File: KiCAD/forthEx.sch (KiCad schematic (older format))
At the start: 33 parts, among them CON1 BARREL_JACK 2,1mm, J1 RCA_JACK, J2 RCA_JACK, J3 PS/2, P1 ICSP, SW1 Power, SW2 reset, U1 LD33V, U2 PIC24FJ64GA002, U3 25LC512, X1 8Mhz

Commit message: first commit
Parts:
- added C12: 100nF, ~, symbol C
- added C7: 10nF, ~, symbol C
- added C8: 22nF, ~, symbol C
- added J3: USB-A_F, symbol USB-A_F
- added R12: 10k, ~, symbol R
- added R7: 4k7, ~, symbol R
- added U4: 23LC1024, symbol 23LC512
- C3, C4: value 22pF -> 18pF
- R9: renamed from R7; value 10K -> 4k7
- U1: value LD33V -> LD1117v33
- U3: value 25LC512 -> 25LC1024
- renumbered C8 to C10, C9 to C11, C7 to C9, J3 to J4, R9 to R10, R10 to R11, R11 to R13, R5 to R2, R2 to R3, R8 to R4, R3 to R5, R4 to R6, R6 to R8
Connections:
- net labels added: ~SS1, ~SS2
- net labels removed: ~SS
- wire segments 104 -> 126
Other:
- note added: "connecteur clavier\n"
- note added: "option 1"
- note added: "option 2"
- moved on the sheet: J1, J4, U3

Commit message: travail sur tvout.s
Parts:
- added D1: 1N6263, symbol DIODESCH
- renumbered D1 to D2, R8 to R10, R7 to R6, R9 to R7, R10 to R8, R6 to R9
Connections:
- wire segments 126 -> 127
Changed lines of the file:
@@
 $EndComp
 $Comp
-L R R9
+L R R7
 U 1 1 55772335
 P 5250 5000
-F 0 "R9" V 5330 5000 40  0000 C CNN
+F 0 "R7" V 5330 5000 40  0000 C CNN
 F 1 "4k7" V 5257 5001 40  0000 C CNN
 F 2 "~" V 5180 5000 30  0000 C CNN
@@
 $EndComp
 $Comp
-L R R6
+L R R9
 U 1 1 557C98D1
 P 7100 2800
-F 0 "R6" V 7180 2800 40  0000 C CNN
+F 0 "R9" V 7180 2800 40  0000 C CNN
 F 1 "10K" V 7107 2801 40  0000 C CNN
 F 2 "~" V 7030 2800 30  0000 C CNN
@@
 $EndComp
 $Comp
-L R R8
+L R R10
 U 1 1 557C98D7
 P 7300 2800
-F 0 "R8" V 7380 2800 40  0000 C CNN
+F 0 "R10" V 7380 2800 40  0000 C CNN
 F 1 "10K" V 7307 2801 40  0000 C CNN
 F 2 "~" V 7230 2800 30  0000 C CNN
@@
 $EndComp
 $Comp
-L LED D1
+L LED D2
 U 1 1 557C9D7F
 P 2800 3200
-F 0 "D1" H 2800 3300 50  0000 C CNN
+F 0 "D2" H 2800 3300 50  0000 C CNN
 F 1 "LED" H 2800 3100 50  0000 C CNN
 F 2 "~" H 2800 3200 60  0000 C CNN
@@
 $EndComp
 $Comp
-L R R10
+L R R8
 U 1 1 557F975C
 P 6000 5250
-F 0 "R10" V 6080 5250 40  0000 C CNN
+F 0 "R8" V 6080 5250 40  0000 C CNN
 F 1 "1K" V 6007 5251 40  0000 C CNN
 F 2 "~" V 5930 5250 30  0000 C CNN
@@
 Text GLabel 4500 3600 0    39   Input ~ 0
 Vidout
-Text GLabel 3000 5900 0    39   Input ~ 0
+Text GLabel 2450 5900 0    39   Input ~ 0
 Vidout
 $Comp
@@
 $EndComp
 $Comp
-L R R7
+L R R6
 U 1 1 5601461A
 P 4750 4550
-F 0 "R7" V 4830 4550 40  0000 C CNN
+F 0 "R6" V 4830 4550 40  0000 C CNN
 F 1 "4k7" V 4757 4551 40  0000 C CNN
 F 2 "~" V 4680 4550 30  0000 C CNN
@@
 	4500 3600 4900 3600
 Wire Wire Line
-	3000 5900 3150 5900
+	2950 5900 3150 5900
 Wire Wire Line
 	6400 3000 6250 3000
@@
 	7300 2350 7300 2550
 Connection ~ 7100 2350
+$Comp
+L DIODESCH D1
+U 1 1 56081043
+P 2750 5900
+F 0 "D1" H 2750 6000 50  0000 C CNN
+F 1 "1N6263" H 2750 5800 50  0000 C CNN
+F 2 "" H 2750 5900 60  0000 C CNN
+F 3 "" H 2750 5900 60  0000 C CNN
+	1    2750 5900
+	1    0    0    -1
+$EndComp
+Wire Wire Line
+	2450 5900 2550 5900
 $EndSCHEMATC

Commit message: travail sur keyboard.s
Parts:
- J4: value PS/2 -> miniDIN-6
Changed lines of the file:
@@
 LIBS:valves
 LIBS:forthEx-cache
-EELAYER 25 0
+EELAYER 27 0
 EELAYER END
 $Descr A4 11693 8268
@@
 Sheet 1 1
 Title ""
-Date "12 sep 2015"
+Date "2 oct 2015"
 Rev ""
 Comp ""
@@
 P 8750 2000
 F 0 "J4" H 8750 1650 60  0000 C CNN
-F 1 "PS/2" H 8750 2450 60  0000 C CNN
+F 1 "miniDIN-6" H 8750 2450 60  0000 C CNN
 F 2 "~" H 8750 2000 60  0000 C CNN
 F 3 "~" H 8750 2000 60  0000 C CNN

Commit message: schematic
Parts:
- removed U2: PIC24FJ64GA002, symbol PIC24FJ64GA002
- added U?: PIC24FJ64GA002, symbol PIC24FJ64GA002
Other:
- moved on the sheet: C10, U1
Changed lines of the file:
@@
 LIBS:valves
 LIBS:forthEx-cache
-EELAYER 27 0
+EELAYER 25 0
 EELAYER END
 $Descr A4 11693 8268
@@
 $EndDescr
 $Comp
-L PIC24FJ64GA002 U2
-U 1 1 5577231C
-P 5600 3750
-F 0 "U2" H 5600 3000 60  0000 C CNN
-F 1 "PIC24FJ64GA002" H 5600 4650 60  0000 C CNN
-F 2 "" H 5600 3750 60  0000 C CNN
-F 3 "" H 5600 3750 60  0000 C CNN
-	1    5600 3750
-	1    0    0    -1
-$EndComp
-$Comp
 L R R7
 U 1 1 55772335
@@
 L C C9
 U 1 1 55772ECC
-P 6750 2650
-F 0 "C9" H 6750 2750 40  0000 L CNN
-F 1 "100nF" H 6756 2565 40  0000 L CNN
-F 2 "~" H 6788 2500 30  0000 C CNN
-F 3 "~" H 6750 2650 60  0000 C CNN
-	1    6750 2650
+P 6900 2650
+F 0 "C9" H 6900 2750 40  0000 L CNN
+F 1 "100nF" H 6906 2565 40  0000 L CNN
+F 2 "~" H 6938 2500 30  0000 C CNN
+F 3 "~" H 6900 2650 60  0000 C CNN
+	1    6900 2650
 	0    -1   -1   0
 $EndComp
@@
 L GND #PWR18
 U 1 1 55772ED2
-P 6950 2850
-F 0 "#PWR18" H 6950 2850 30  0001 C CNN
-F 1 "GND" H 6950 2780 30  0001 C CNN
-F 2 "" H 6950 2850 60  0000 C CNN
-F 3 "" H 6950 2850 60  0000 C CNN
-	1    6950 2850
+P 7100 2850
+F 0 "#PWR18" H 7100 2850 30  0001 C CNN
+F 1 "GND" H 7100 2780 30  0001 C CNN
+F 2 "" H 7100 2850 60  0000 C CNN
+F 3 "" H 7100 2850 60  0000 C CNN
+	1    7100 2850
 	1    0    0    -1
 $EndComp
@@
 L CAPAPOL C10
 U 1 1 55773066
-P 6850 3800
-F 0 "C10" H 6900 3900 40  0000 L CNN
-F 1 "47µF" H 6900 3700 40  0000 L CNN
-F 2 "~" H 6950 3650 30  0000 C CNN
-F 3 "~" H 6850 3800 300 0000 C CNN
-	1    6850 3800
+P 7000 3800
+F 0 "C10" H 7050 3900 40  0000 L CNN
+F 1 "47µF" H 7050 3700 40  0000 L CNN
+F 2 "~" H 7100 3650 30  0000 C CNN
+F 3 "~" H 7000 3800 300 0000 C CNN
+	1    7000 3800
 	0    -1   -1   0
 $EndComp
@@
 L GND #PWR19
 U 1 1 55773073
-P 7200 4150
-F 0 "#PWR19" H 7200 4150 30  0001 C CNN
-F 1 "GND" H 7200 4080 30  0001 C CNN
-F 2 "" H 7200 4150 60  0000 C CNN
-F 3 "" H 7200 4150 60  0000 C CNN
-	1    7200 4150
+P 7350 4150
+F 0 "#PWR19" H 7350 4150 30  0001 C CNN
+F 1 "GND" H 7350 4080 30  0001 C CNN
+F 2 "" H 7350 4150 60  0000 C CNN
+F 3 "" H 7350 4150 60  0000 C CNN
+	1    7350 4150
 	1    0    0    -1
 $EndComp
@@
 Text GLabel 9350 2250 2    39   Input ~ 0
 KBDAT
-Text GLabel 7450 3300 2    39   Input ~ 0
+Text GLabel 7600 3300 2    39   Input ~ 0
 KBCLK
-Text GLabel 7450 3200 2    39   Input ~ 0
+Text GLabel 7600 3200 2    39   Input ~ 0
 KBDAT
 $Comp
@@
 	1    0    0    -1
 $EndComp
-Text GLabel 6400 4000 2    39   Input ~ 0
+Text GLabel 6550 4000 2    39   Input ~ 0
 ~SS1
-Text GLabel 6400 4100 2    39   Input ~ 0
+Text GLabel 6550 4100 2    39   Input ~ 0
 SCLK
-Text GLabel 6400 4200 2    39   Input ~ 0
+Text GLabel 6550 4200 2    39   Input ~ 0
 MISO
-Text GLabel 6400 4300 2    39   Input ~ 0
+Text GLabel 6550 4300 2    39   Input ~ 0
 MOSI
 Text GLabel 8550 3500 0    39   Input ~ 0
@@
 L R R9
 U 1 1 557C98D1
-P 7100 2800
-F 0 "R9" V 7180 2800 40  0000 C CNN
-F 1 "10K" V 7107 2801 40  0000 C CNN
-F 2 "~" V 7030 2800 30  0000 C CNN
-F 3 "~" H 7100 2800 30  0000 C CNN
-	1    7100 2800
+P 7250 2800
+F 0 "R9" V 7330 2800 40  0000 C CNN
+F 1 "10K" V 7257 2801 40  0000 C CNN
+F 2 "~" V 7180 2800 30  0000 C CNN
+F 3 "~" H 7250 2800 30  0000 C CNN
+	1    7250 2800
 	-1   0    0    1
 $EndComp
@@
 L R R10
 U 1 1 557C98D7
-P 7300 2800
-F 0 "R10" V 7380 2800 40  0000 C CNN
-F 1 "10K" V 7307 2801 40  0000 C CNN
-F 2 "~" V 7230 2800 30  0000 C CNN
-F 3 "~" H 7300 2800 30  0000 C CNN
-	1    7300 2800
+P 7450 2800
+F 0 "R10" V 7530 2800 40  0000 C CNN
+F 1 "10K" V 7457 2801 40  0000 C CNN
+F 2 "~" V 7380 2800 30  0000 C CNN
+F 3 "~" H 7450 2800 30  0000 C CNN
+	1    7450 2800
 	-1   0    0    1
 $EndComp
@@
 L LD33V U1
 U 1 1 557CCDC4
-P 2000 1150
-F 0 "U1" H 2000 1450 60  0000 C CNN
-F 1 "LD1117v33" H 2000 1350 60  0000 C CNN
-F 2 "" H 2000 1150 60  0000 C CNN
-F 3 "" H 2000 1150 60  0000 C CNN
-	1    2000 1150
+P 2000 1400
+F 0 "U1" H 2000 1700 60  0000 C CNN
+F 1 "LD1117v33" H 2000 2000 60  0000 C CNN
+F 2 "" H 2000 1400 60  0000 C CNN
+F 3 "" H 2000 1400 60  0000 C CNN
+	1    2000 1400
 	1    0    0    -1
 $EndComp
@@
 Text GLabel 8950 4450 1    39   Input ~ 0
 +3V
-Text GLabel 6400 3700 2    39   Input ~ 0
+Text GLabel 6550 3700 2    39   Input ~ 0
 ~SS2
 $Comp
@@
 Connection ~ 3600 2350
 Wire Wire Line
-	6400 2350 6400 3000
+	6550 2350 6550 3000
 Connection ~ 4650 2350
 Wire Wire Line
-	6950 2650 6950 2850
-Wire Wire Line
-	6550 2650 6400 2650
-Connection ~ 6400 2650
-Wire Wire Line
-	6250 3100 6850 3100
-Wire Wire Line
-	6850 3100 6850 2800
-Connection ~ 6950 2800
+	7100 2650 7100 2850
+Wire Wire Line
+	6700 2650 6550 2650
+Connection ~ 6550 2650
+Wire Wire Line
+	6400 3100 7000 3100
+Wire Wire Line
+	7000 3100 7000 2800
+Connection ~ 7100 2800
 Wire Wire Line
 	4200 4600 4200 4700
@@
 	4050 4200 4900 4200
 Wire Wire Line
-	7200 3800 7200 4150
-Wire Wire Line
-	7200 3800 7050 3800
-Wire Wire Line
-	6650 3800 6250 3800
-Connection ~ 7200 4000
-Connection ~ 6400 2350
+	7350 3800 7350 4150
+Wire Wire Line
+	7350 3800 7200 3800
+Wire Wire Line
+	6800 3800 6400 3800
+Connection ~ 7350 4000
+Connection ~ 6550 2350
 Wire Wire Line
 	2800 4450 2800 4600
@@
 	3650 5900 4650 5900
 Wire Wire Line
-	6400 4000 6250 4000
+	6550 4000 6400 4000
 Wire Wire Line
 	8550 3500 9050 3500
@@
 	1400 2250 1750 2250
 Wire Wire Line
-	6750 4000 7200 4000
-Wire Wire Line
-	6750 4000 6750 3900
-Wire Wire Line
-	6750 3900 6250 3900
-Wire Wire Line
-	6250 4300 6400 4300
-Wire Wire Line
-	6250 4100 6400 4100
-Wire Wire Line
-	6400 4200 6250 4200
+	6900 4000 7350 4000
+Wire Wire Line
+	6900 4000 6900 3900
+Wire Wire Line
+	6900 3900 6400 3900
+Wire Wire Line
+	6400 4300 6550 4300
+Wire Wire Line
+	6400 4100 6550 4100
+Wire Wire Line
+	6550 4200 6400 4200
 Wire Wire Line
 	8950 3450 8950 3500
@@
 	6900 5500 6900 5600
 Wire Wire Line
-	6850 2800 6950 2800
+	7000 2800 7100 2800
 Wire Wire Line
 	4700 3300 4900 3300
@@
 	2950 5900 3150 5900
 Wire Wire Line
-	6400 3000 6250 3000
+	6550 3000 6400 3000
 Connection ~ 4750 3000
 Wire Wire Line
@@
 Connection ~ 8850 4600
 Wire Wire Line
-	6250 3700 6400 3700
+	6400 3700 6550 3700
 Wire Wire Line
 	8200 1100 8100 1100
@@
 Connection ~ 2800 2350
 Wire Wire Line
-	2750 2350 7300 2350
+	2750 2350 7450 2350
 Wire Wire Line
 	7950 1950 8050 1950
@@
 	5650 5400 5650 5450
 Wire Wire Line
-	6250 3300 7450 3300
-Wire Wire Line
-	6250 3200 7450 3200
-Wire Wire Line
-	7100 3050 7100 3200
-Connection ~ 7100 3200
-Wire Wire Line
-	7300 3050 7300 3300
-Connection ~ 7300 3300
-Wire Wire Line
-	7100 2350 7100 2550
-Wire Wire Line
-	7300 2350 7300 2550
-Connection ~ 7100 2350
+	6400 3300 7600 3300
+Wire Wire Line
+	6400 3200 7600 3200
+Wire Wire Line
+	7250 3050 7250 3200
+Connection ~ 7250 3200
+Wire Wire Line
+	7450 3050 7450 3300
+Connection ~ 7450 3300
+Wire Wire Line
+	7250 2350 7250 2550
+Wire Wire Line
+	7450 2350 7450 2550
+Connection ~ 7250 2350
 $Comp
 L DIODESCH D1
@@
 Wire Wire Line
 	2450 5900 2550 5900
+$Comp
+L PIC24FJ64GA002 U?
+U 1 1 5612D809
+P 5700 3700
+F 0 "U?" H 5700 2950 60  0000 C CNN
+F 1 "PIC24FJ64GA002" H 5750 4500 60  0000 C CNN
+F 2 "" H 5700 3700 60  0000 C CNN
+F 3 "" H 5700 3700 60  0000 C CNN
+	1    5700 3700
+	1    0    0    -1
+$EndComp
 $EndSCHEMATC

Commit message: schématique ajout rs-232
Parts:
- added C2: 33µF, ~, symbol CAPAPOL
- added D1: 1N6263, symbol DIODESCH
- added Q1: 2N3906, symbol PNP
- added Q2: 2N3904, symbol NPN
- added R1: 3K3, symbol R
- added R2, R3: 47K, symbol R
- added R4: 10k, symbol R
- gave numbers to parts that had none: 1
- renumbered C9 to C10, C10 to C11, C11 to C12, C12 to C13, C2 to C3, C3 to C4, C4 to C5, C5 to C6, C6 to C7, C7 to C8, C8 to C9, D1 to D3, R4 to R10, R7 to R11, R8 to R12, R9 to R13, R10 to R14, R11 to R15, R12 to R16, R13 to R17, R1 to R5, R3 to R6, R5 to R7, R6 to R8, R2 to R9
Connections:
- net labels added: RS232-RX, RS232-TX, RX, TX
- wire segments 127 -> 144
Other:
- note added: "RS232\nconverter"
- note added: "UART"
- moved on the sheet: D3, J1

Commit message: changement de processeur
adaptation matérielle et logicielle
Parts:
- C10, C12, C13, C3, C4, C5, C6, C7, C8, C9: symbol C -> C-RESCUE-forthEx
- D2: symbol LED -> LED-RESCUE-forthEx
- R1, R10, R11, R12, R13, R14, R15, R16, R17, R2, R3, R4, R5, R6, R7, R8, R9: symbol R -> R-RESCUE-forthEx
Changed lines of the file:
@@
 EESchema Schematic File Version 2
+LIBS:forthEx-rescue
 LIBS:power
 LIBS:device
@@
 LIBS:memory
 LIBS:xilinx
-LIBS:special
 LIBS:microcontrollers
 LIBS:dsp
@@
 $EndDescr
 $Comp
-L R R11
+L R-RESCUE-forthEx R11
 U 1 1 55772335
 P 5250 5000
@@
 $EndComp
 $Comp
-L R R9
+L R-RESCUE-forthEx R9
 U 1 1 557723B5
 P 4700 6600
@@
 $EndComp
 $Comp
-L R R10
+L R-RESCUE-forthEx R10
 U 1 1 557723D1
 P 5100 6250
@@
 $EndComp
 $Comp
-L R R7
+L R-RESCUE-forthEx R7
 U 1 1 557729D3
 P 4150 3000
@@
 $EndComp
 $Comp
-L R R6
+L R-RESCUE-forthEx R6
 U 1 1 557729E0
 P 3600 2750
@@
 $EndComp
 $Comp
-L C C6
+L C-RESCUE-forthEx C6
 U 1 1 557729E8
 P 3600 3300
@@
 +3V
 $Comp
-L C C7
+L C-RESCUE-forthEx C7
 U 1 1 55772EC6
 P 4200 4400
@@
 $EndComp
 $Comp
-L C C10
+L C-RESCUE-forthEx C10
 U 1 1 55772ECC
 P 6900 2650
@@
 $EndComp
 $Comp
-L C C5
+L C-RESCUE-forthEx C5
 U 1 1 557736BE
 P 3400 4250
@@
 $EndComp
 $Comp
-L C C4
+L C-RESCUE-forthEx C4
 U 1 1 557736CB
 P 2800 4250
@@
 $EndComp
 $Comp
-L C C12
+L C-RESCUE-forthEx C12
 U 1 1 55773ACD
 P 10400 3500
@@
 $EndComp
 $Comp
-L R R15
+L R-RESCUE-forthEx R15
 U 1 1 55773BD0
 P 8700 3200
@@
 	1    0    0    -1
 $EndComp
+Text GLabel 6550 4300 2    39   Input ~ 0
+~SS1
+Text GLabel 6550 4200 2    39   Input ~ 0
+SCLK
 Text GLabel 6550 4000 2    39   Input ~ 0
-~SS1
+MISO
 Text GLabel 6550 4100 2    39   Input ~ 0
-SCLK
-Text GLabel 6550 4200 2    39   Input ~ 0
-MISO
-Text GLabel 6550 4300 2    39   Input ~ 0
 MOSI
 Text GLabel 8550 3500 0    39   Input ~ 0
@@
 $EndComp
 $Comp
-L R R17
+L R-RESCUE-forthEx R17
 U 1 1 55778C04
 P 8950 3200
@@
 $EndComp
 $Comp
-L R R13
+L R-RESCUE-forthEx R13
 U 1 1 557C98D1
 P 7250 2800
@@
 $EndComp
 $Comp
-L R R14
+L R-RESCUE-forthEx R14
 U 1 1 557C98D7
 P 7450 2800
@@
 $EndComp
 $Comp
-L R R5
+L R-RESCUE-forthEx R5
 U 1 1 557C9D70
 P 2800 2650
@@
 $EndComp
 $Comp
-L LED D2
+L LED-RESCUE-forthEx D2
 U 1 1 557C9D7F
 P 2800 3200
@@
 $EndComp
 $Comp
-L C C3
+L C-RESCUE-forthEx C3
 U 1 1 557CC8BB
 P 2400 1050
@@
 $EndComp
 $Comp
-L R R12
+L R-RESCUE-forthEx R12
 U 1 1 557F975C
 P 6000 5250
@@
 $EndComp
 $Comp
-L C C13
+L C-RESCUE-forthEx C13
 U 1 1 55FA145F
 P 10400 5250
@@
 $EndComp
 $Comp
-L R R16
+L R-RESCUE-forthEx R16
 U 1 1 55FA147B
 P 8700 4950
@@
 $EndComp
 $Comp
-L R R8
+L R-RESCUE-forthEx R8
 U 1 1 5601461A
 P 4750 4550
@@
 $EndComp
 $Comp
-L C C8
+L C-RESCUE-forthEx C8
 U 1 1 5601470A
 P 4750 5200
@@
 $EndComp
 $Comp
-L C C9
+L C-RESCUE-forthEx C9
 U 1 1 56014795
 P 5650 5200
@@
 $EndComp
 $Comp
-L R R2
+L R-RESCUE-forthEx R2
 U 1 1 5613C08F
 P 2000 6400
@@
 $EndComp
 $Comp
-L R R4
+L R-RESCUE-forthEx R4
 U 1 1 5613F420
 P 2700 5900
@@
 $EndComp
 $Comp
-L R R1
+L R-RESCUE-forthEx R1
 U 1 1 5613F63B
 P 1500 5950
@@
 $EndComp
 $Comp
-L R R3
+L R-RESCUE-forthEx R3
 U 1 1 5613F821
 P 2150 5400
@@
 	4950 6600 5950 6600
 Wire Wire Line
-	6550 4000 6400 4000
+	6550 4300 6400 4300
 Wire Wire Line
 	8550 3500 9050 3500
@@
 	6900 3900 6400 3900
 Wire Wire Line
-	6400 4300 6550 4300
-Wire Wire Line
 	6400 4100 6550 4100
 Wire Wire Line
-	6550 4200 6400 4200
+	6400 4200 6550 4200
+Wire Wire Line
+	6550 4000 6400 4000
 Wire Wire Line
 	8950 3450 8950 3500
@@
 Wire Wire Line
 	1100 6550 1050 6550
-Text GLabel 6550 3400 2    39   Input ~ 0
+Text GLabel 6550 3600 2    39   Input ~ 0
 TX
 Text GLabel 6550 3500 2    39   Input ~ 0
@@
 	6550 3500 6400 3500
 Wire Wire Line
-	6550 3400 6400 3400
-Text Notes 6750 3500 0    39   ~ 0
+	6550 3600 6400 3600
+Text Notes 6750 3600 0    39   ~ 0
 UART
 Text Notes 1950 7050 0    39   ~ 0

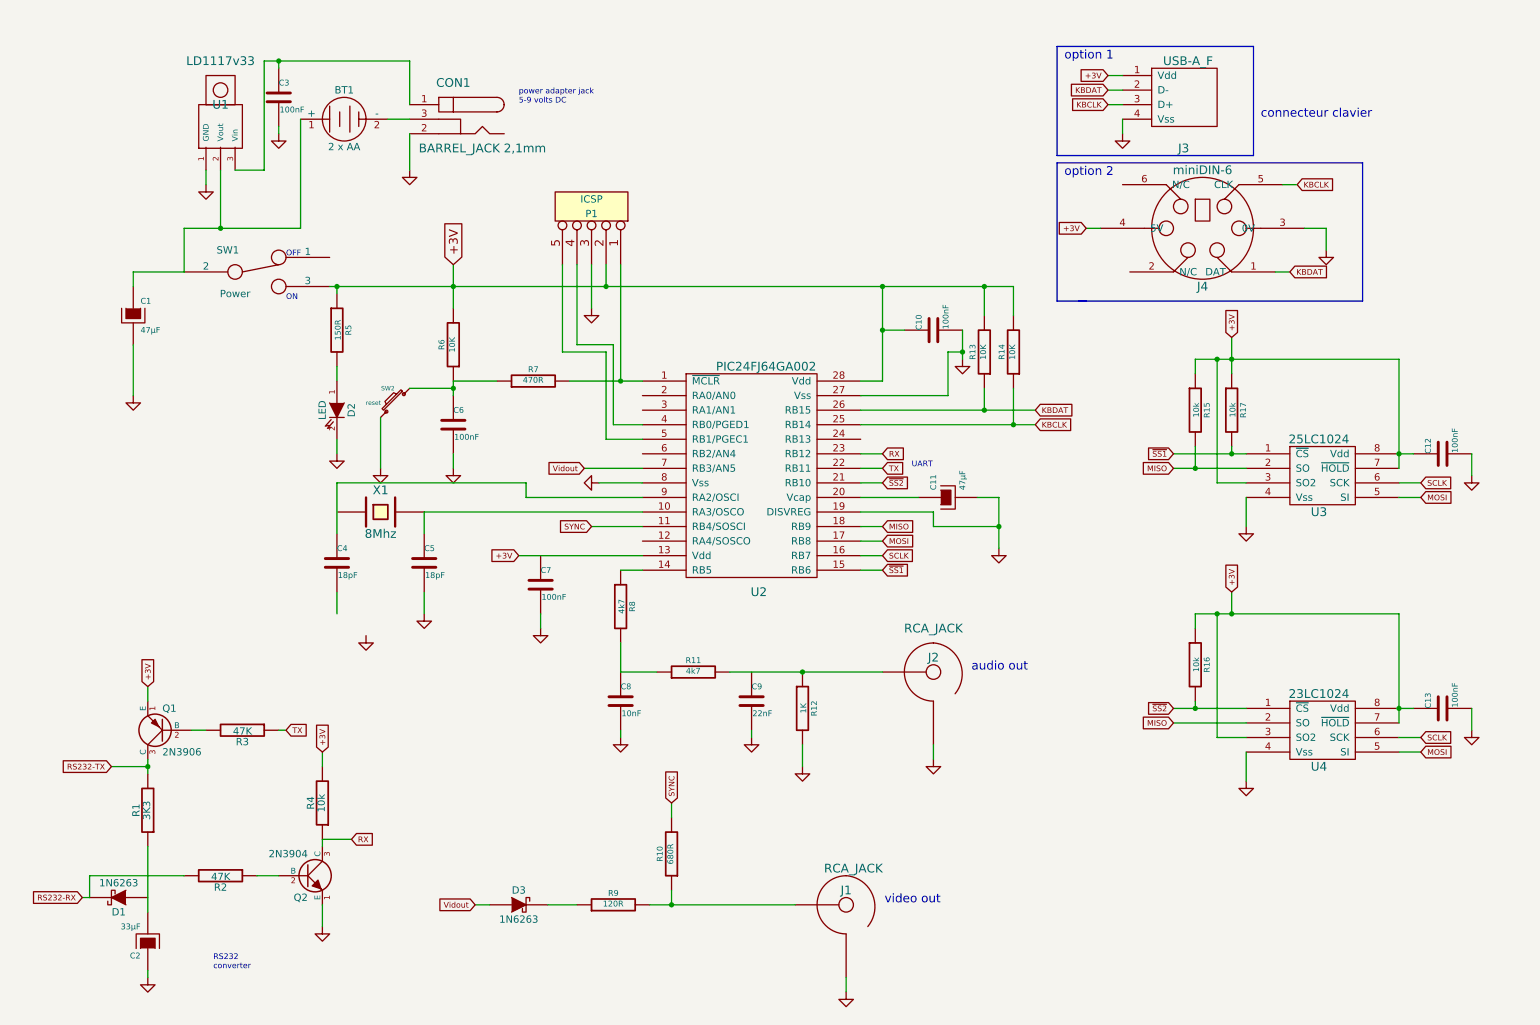
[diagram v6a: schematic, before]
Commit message: modification schématique
enlevé support pile
ajout régulateur 5 volt pour clavier
ajout support carte SD
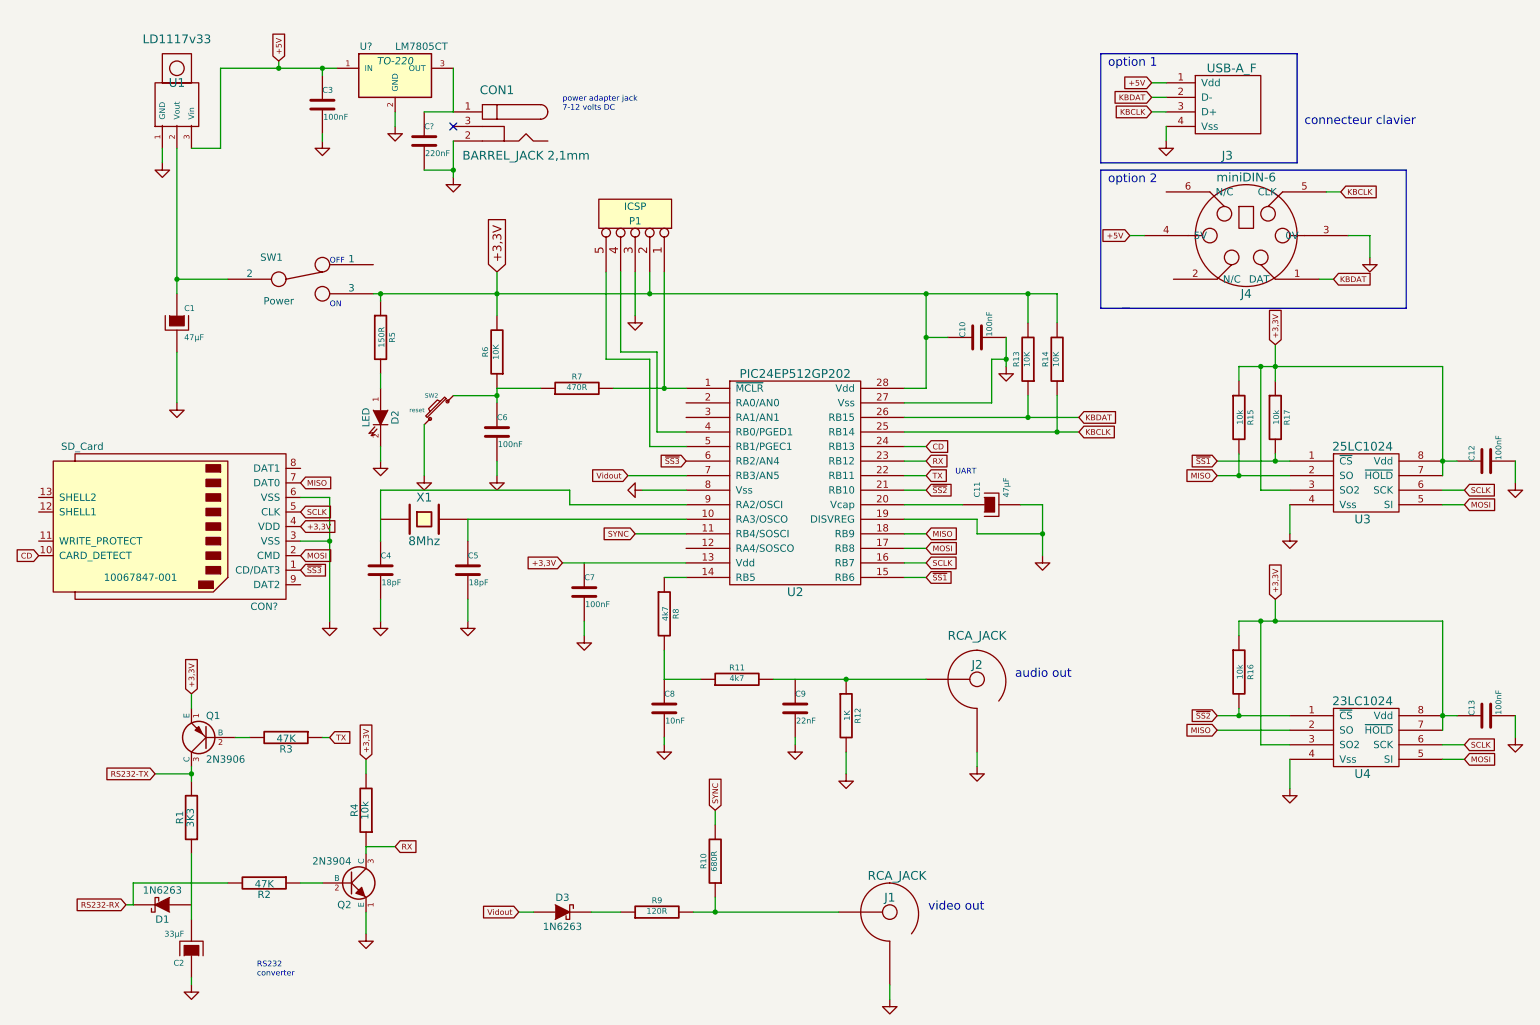
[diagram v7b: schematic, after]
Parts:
- removed BT1: 2 x AA, ~, symbol BATTERY
- added C?: 220nF, ~, symbol C-RESCUE-forthEx
- added CON?: SD_Card, 10067847-001, symbol SD_Card
- added U?: LM7805CT, TO-220, symbol LM7805CT
- U2: value PIC24FJ64GA002 -> PIC24EP512GP202
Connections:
- net GND: now also C4.2, C?.2, CON?.3 (VSS), CON?.6 (VSS), U?.2 (GND)
- net MISO: now also CON?.7 (DAT0)
- net MOSI: now also CON?.2 (CMD)
- net SCLK: now also CON?.5 (CLK)
- net +5V: now reaches C3.1, U1.3 (Vin)
- net +5V: now also J3.1 (Vdd), J4.4 (5V), U?.1 (IN); no longer CON1.1
- net CD: now reaches U2.24 (RB13)
- net CD: now also CON?.10 (CARD_DETECT)
- net ~SS3: now reaches U2.6 (RB2/AN4)
- net ~SS3: now also CON?.1 (CD/DAT3)
- net +3V renamed +3,3V
- net +3,3V: now also CON?.4 (VDD); no longer J3.1 (Vdd), J4.4 (5V)
- new net: C?.1, CON1.1, U?.3 (OUT)
- no-connect marks 0 -> 1
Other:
- note added: "power adapter jack\n7-12 volts DC"
- note removed: "power adapter jack\n5-9 volts DC"
- moved on the sheet: C1, C10, C11, C12, C13, C2, C3, C4, C5, C6, C7, C8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
